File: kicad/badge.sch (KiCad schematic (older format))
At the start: 13 parts, among them IC1 ATMEGA328-P, P1 CONN_01X07, P2 9v battery, P3 FTDI programmer, SW1 SPST, U1 LM7805, Y1 16Mhz

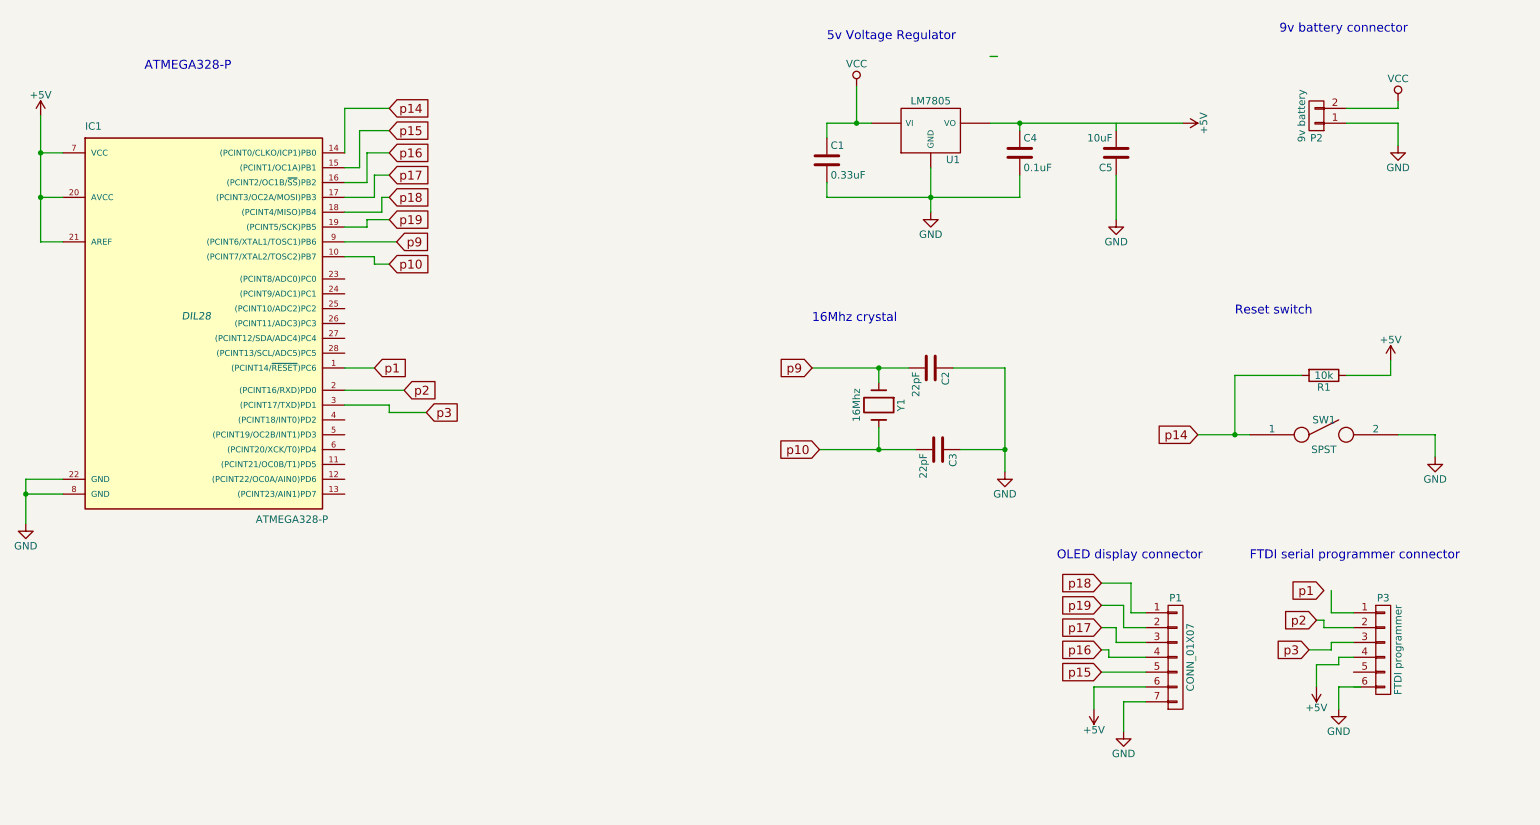
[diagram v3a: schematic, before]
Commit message: fix problems from rule check
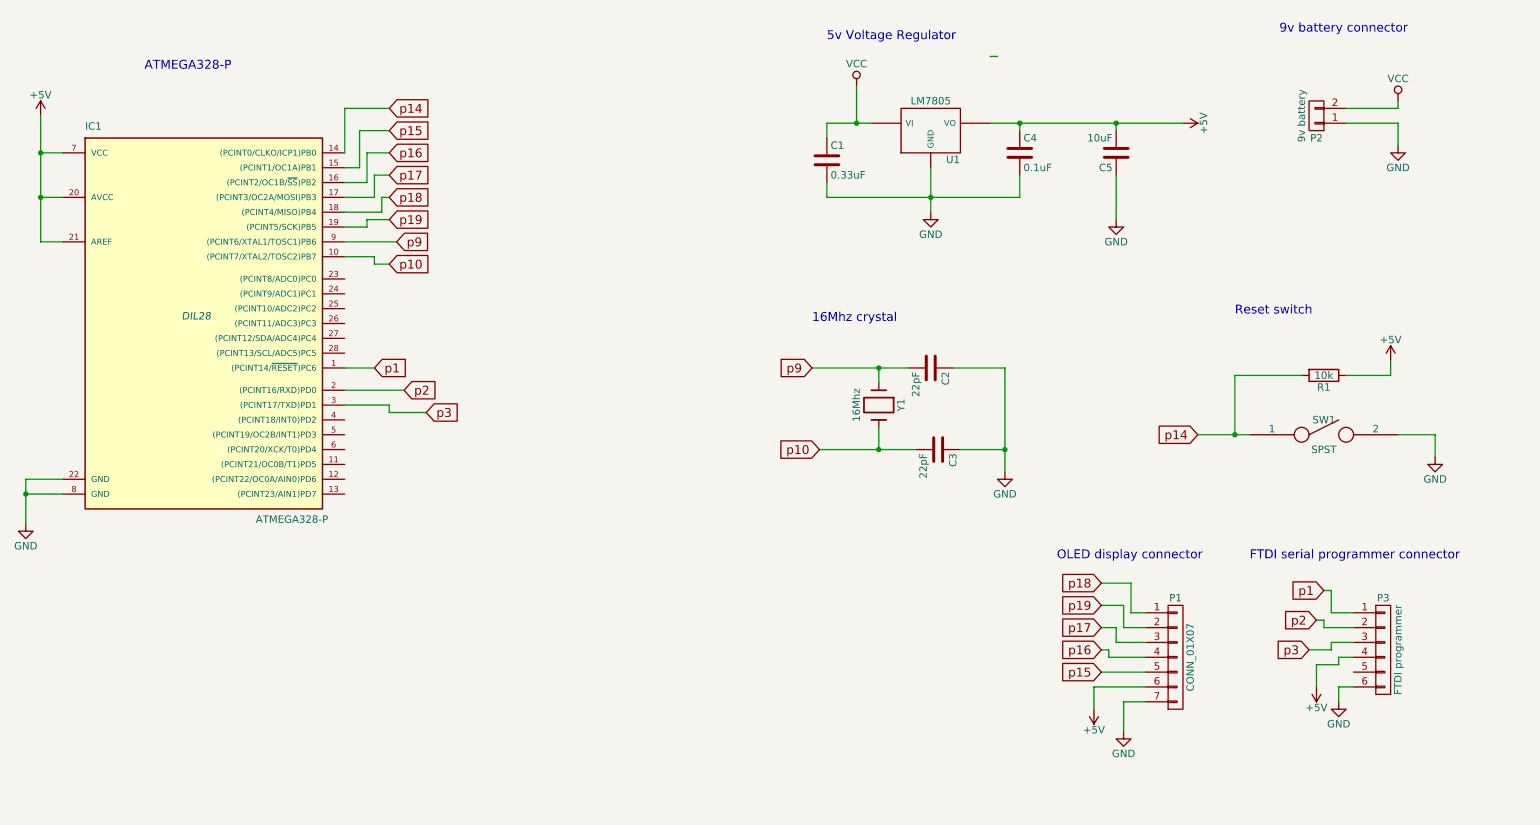
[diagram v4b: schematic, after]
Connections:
- wire segments 94 -> 107
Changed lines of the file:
@@
 L GND #PWR08
 U 1 1 58E1B9A0
-P 9950 5400
-F 0 "#PWR08" H 9950 5150 50  0001 C CNN
-F 1 "GND" H 9950 5250 50  0000 C CNN
-F 2 "" H 9950 5400 50  0000 C CNN
-F 3 "" H 9950 5400 50  0000 C CNN
-	1    9950 5400
+P 9950 5350
+F 0 "#PWR08" H 9950 5100 50  0001 C CNN
+F 1 "GND" H 9950 5200 50  0000 C CNN
+F 2 "" H 9950 5350 50  0000 C CNN
+F 3 "" H 9950 5350 50  0000 C CNN
+	1    9950 5350
 	1    0    0    -1
 $EndComp
@@
 	7350 3100 7700 3100
 Wire Wire Line
-	7700 3100 7700 3800
-Wire Wire Line
 	7400 3650 7700 3650
-Connection ~ 7700 3650
 Wire Wire Line
 	1350 3950 1100 3950
@@
 	8450 1800 8450 2100
 Wire Wire Line
-	9000 3550 9350 3550
+	9000 3550 9250 3550
+Wire Wire Line
+	9250 3550 9350 3550
 Wire Wire Line
 	9700 3150 9250 3150
@@
 	10300 3150 10000 3150
 Wire Wire Line
-	6500 1450 6800 1450
+	6500 1450 6700 1450
+Wire Wire Line
+	6700 1450 6800 1450
 Wire Wire Line
 	6500 1450 6500 1550
 Wire Wire Line
-	7200 1750 7200 2050
+	7200 1750 7200 1950
+Wire Wire Line
+	7200 1950 7200 2050
 Wire Wire Line
 	6500 1850 6500 1950
 Wire Wire Line
-	6500 1950 7800 1950
+	6500 1950 7200 1950
+Wire Wire Line
+	7200 1950 7800 1950
 Connection ~ 7200 1950
 Wire Wire Line
 	7800 1950 7800 1800
 Wire Wire Line
-	7600 1450 8900 1450
+	7600 1450 7800 1450
+Wire Wire Line
+	7800 1450 8450 1450
+Wire Wire Line
+	8450 1450 8900 1450
 Wire Wire Line
 	7800 1450 7800 1500
@@
 Wire Wire Line
 	10300 3050 10300 3150
-Wire Wire Line
-	6700 1200 6700 1450
 Connection ~ 6700 1450
 Connection ~ 6850 3100
 Connection ~ 6850 3650
 Wire Wire Line
-	1100 3850 1100 4150
+	1100 3850 1100 3950
+Wire Wire Line
+	1100 3950 1100 4150
 Wire Wire Line
 	10350 3550 10600 3550
@@
 	10000 1350 10350 1350
 Wire Wire Line
-	10350 1350 10350 1300
-Wire Wire Line
 	10000 1450 10350 1450
 Wire Wire Line
 	10350 1450 10350 1600
 Wire Wire Line
-	10100 5250 9950 5250
-Wire Wire Line
-	9950 5250 9950 5400
-Wire Wire Line
 	10600 3550 10600 3700
 Wire Wire Line
@@
 	9900 4600 9900 4750
 Wire Wire Line
-	9900 4750 10050 4750
-Wire Wire Line
 	9800 4800 9850 4800
 Wire Wire Line
@@
 Wire Wire Line
 	9950 5050 10050 5050
-Wire Wire Line
-	8450 1450 8450 1500
-Wire Wire Line
-	1200 2250 1350 2250
 Wire Wire Line
 	1200 1950 1350 1950
@@
 	1200 1650 1350 1650
 Wire Wire Line
-	1200 1400 1200 2250
+	1200 1400 1200 1650
+Wire Wire Line
+	1200 1650 1200 1950
+Wire Wire Line
+	1200 1950 1200 2250
 $Comp
 L +5V #PWR013
@@
 Reset switch
 Wire Wire Line
-	6400 3100 7050 3100
-Wire Wire Line
-	6450 3650 7100 3650
+	6400 3100 6850 3100
+Wire Wire Line
+	6850 3100 7050 3100
+Wire Wire Line
+	6450 3650 6850 3650
+Wire Wire Line
+	6850 3650 7100 3650
 $Comp
 L GND #PWR014
@@
 Wire Wire Line
 	3450 2400 3550 2400
+Wire Wire Line
+	7700 3100 7700 3650
+Wire Wire Line
+	7700 3650 7700 3800
+Connection ~ 7700 3650
+Wire Wire Line
+	10350 1350 10350 1300
+Wire Wire Line
+	8450 1450 8450 1500
+Connection ~ 8450 1450
+Wire Wire Line
+	9850 4600 9900 4600
+Wire Wire Line
+	10050 5250 9950 5250
+Wire Wire Line
+	9900 4750 10050 4750
+Wire Wire Line
+	1200 2250 1350 2250
+Wire Wire Line
+	6700 1200 6700 1450
+Wire Wire Line
+	9950 5250 9950 5350
 $EndSCHEMATC

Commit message: add LEDs
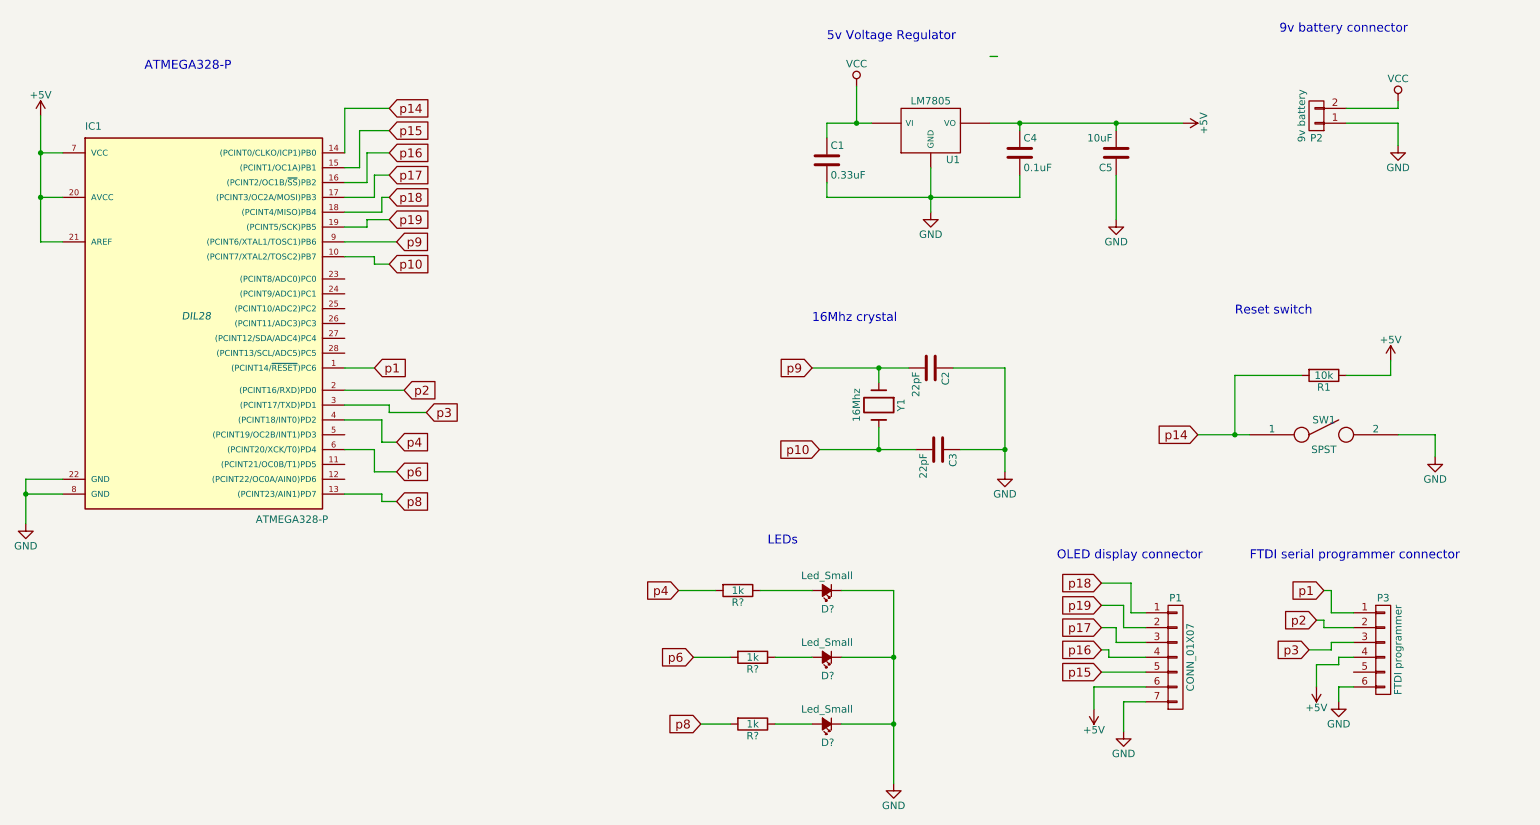
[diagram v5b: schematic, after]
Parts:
- added D? (x3): Led_Small, symbol Led_Small
- added R? (x3): 1k, symbol R
- C5: footprint (none) -> Capacitors_ThroughHole:C_Rect_L7_W2.5_P5
- P1: footprint (none) -> Pin_Headers:Pin_Header_Straight_1x07
- P2: footprint (none) -> Pin_Headers:Pin_Header_Straight_1x02
- P3: footprint (none) -> Pin_Headers:Pin_Header_Straight_1x06
- R1: footprint (none) -> Resistors_ThroughHole:Resistor_Horizontal_RM10mm
- SW1: footprint (none) -> Buttons_Switches_ThroughHole:SW_PUSH_SMALL
- Y1: footprint (none) -> Crystals:Crystal_HC49-U_Vertical
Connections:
- net GND: now also D?.1 (K), D?.1 (K), D?.1 (K)
- net p8: now reaches IC1.13 ((PCINT23/AIN1)PD7)
- net p8: now also R?.2
- net p4: now reaches IC1.4 ((PCINT18/INT0)PD2)
- net p4: now also R?.2
- net p6: now reaches IC1.6 ((PCINT20/XCK/T0)PD4)
- net p6: now also R?.2
- new net: D?.2 (A), R?.1 (x3)
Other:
- note added: "LEDs\n"
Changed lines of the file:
@@
 F 0 "R1" V 9930 3150 50  0000 C CNN
 F 1 "10k" V 9850 3150 50  0000 C CNN
-F 2 "" V 9780 3150 50  0000 C CNN
+F 2 "Resistors_ThroughHole:Resistor_Horizontal_RM10mm" V 9780 3150 50  0001 C CNN
 F 3 "" H 9850 3150 50  0000 C CNN
 	1    9850 3150
@@
 F 0 "C2" H 7225 3200 50  0000 L CNN
 F 1 "22pF" H 7225 3000 50  0000 L CNN
-F 2 "" H 7238 2950 50  0000 C CNN
+F 2 "" H 7238 2950 50  0001 C CNN
 F 3 "" H 7200 3100 50  0000 C CNN
 	1    7200 3100
@@
 F 0 "C5" H 8475 1750 50  0000 L CNN
 F 1 "10uF" H 8475 1550 50  0000 L CNN
-F 2 "" H 8488 1500 50  0000 C CNN
+F 2 "Capacitors_ThroughHole:C_Rect_L7_W2.5_P5" H 8488 1500 50  0001 C CNN
 F 3 "" H 8450 1650 50  0000 C CNN
 	1    8450 1650
@@
 F 0 "SW1" H 9850 3650 50  0000 C CNN
 F 1 "SPST" H 9850 3450 50  0000 C CNN
-F 2 "" H 9850 3550 50  0000 C CNN
+F 2 "Buttons_Switches_ThroughHole:SW_PUSH_SMALL" H 9850 3550 50  0001 C CNN
 F 3 "" H 9850 3550 50  0000 C CNN
 	1    9850 3550
@@
 F 0 "U1" H 7350 1304 50  0000 C CNN
 F 1 "LM7805" H 7200 1700 50  0000 C CNN
-F 2 "" H 7200 1500 50  0000 C CNN
+F 2 "" H 7200 1500 50  0001 C CNN
 F 3 "" H 7200 1500 50  0000 C CNN
 	1    7200 1500
@@
 F 0 "C4" H 7825 1750 50  0000 L CNN
 F 1 "0.1uF" H 7825 1550 50  0000 L CNN
-F 2 "" H 7838 1500 50  0000 C CNN
+F 2 "" H 7838 1500 50  0001 C CNN
 F 3 "" H 7800 1650 50  0000 C CNN
 	1    7800 1650
@@
 F 0 "C1" H 6525 1800 50  0000 L CNN
 F 1 "0.33uF" H 6525 1600 50  0000 L CNN
-F 2 "" H 6538 1550 50  0000 C CNN
+F 2 "" H 6538 1550 50  0001 C CNN
 F 3 "" H 6500 1700 50  0000 C CNN
 	1    6500 1700
@@
 F 0 "P2" H 9800 1550 50  0000 C CNN
 F 1 "9v battery " V 9900 1400 50  0000 C CNN
-F 2 "" H 9800 1400 50  0000 C CNN
+F 2 "Pin_Headers:Pin_Header_Straight_1x02" H 9800 1400 50  0001 C CNN
 F 3 "" H 9800 1400 50  0000 C CNN
 	1    9800 1400
@@
 F 0 "P3" H 10250 5350 50  0000 C CNN
 F 1 "FTDI programmer" V 10350 5000 50  0000 C CNN
-F 2 "" H 10250 5000 50  0000 C CNN
+F 2 "Pin_Headers:Pin_Header_Straight_1x06" H 10250 5000 50  0001 C CNN
 F 3 "" H 10250 5000 50  0000 C CNN
 	1    10250 5000
@@
 F 0 "Y1" H 6850 3500 50  0000 C CNN
 F 1 "16Mhz" H 6850 3200 50  0000 C CNN
-F 2 "" H 6850 3350 50  0000 C CNN
+F 2 "Crystals:Crystal_HC49-U_Vertical" H 6850 3350 50  0001 C CNN
 F 3 "" H 6850 3350 50  0000 C CNN
 	1    6850 3350
@@
 F 0 "C3" H 7275 3750 50  0000 L CNN
 F 1 "22pF" H 7275 3550 50  0000 L CNN
-F 2 "" H 7288 3500 50  0000 C CNN
+F 2 "" H 7288 3500 50  0001 C CNN
 F 3 "" H 7250 3650 50  0000 C CNN
 	1    7250 3650
@@
 	8450 1800 8450 2100
 Wire Wire Line
-	9000 3550 9250 3550
-Wire Wire Line
-	9250 3550 9350 3550
+	9000 3550 9350 3550
 Wire Wire Line
 	9700 3150 9250 3150
@@
 	10300 3150 10000 3150
 Wire Wire Line
-	6500 1450 6700 1450
-Wire Wire Line
-	6700 1450 6800 1450
+	6500 1450 6800 1450
 Wire Wire Line
 	6500 1450 6500 1550
 Wire Wire Line
-	7200 1750 7200 1950
-Wire Wire Line
-	7200 1950 7200 2050
+	7200 1750 7200 2050
 Wire Wire Line
 	6500 1850 6500 1950
 Wire Wire Line
-	6500 1950 7200 1950
-Wire Wire Line
-	7200 1950 7800 1950
+	6500 1950 7800 1950
 Connection ~ 7200 1950
 Wire Wire Line
 	7800 1950 7800 1800
 Wire Wire Line
-	7600 1450 7800 1450
-Wire Wire Line
-	7800 1450 8450 1450
-Wire Wire Line
-	8450 1450 8900 1450
+	7600 1450 8900 1450
 Wire Wire Line
 	7800 1450 7800 1500
@@
 Connection ~ 6850 3650
 Wire Wire Line
-	1100 3850 1100 3950
-Wire Wire Line
-	1100 3950 1100 4150
+	1100 3850 1100 4150
 Wire Wire Line
 	10350 3550 10600 3550
@@
 	1200 1650 1350 1650
 Wire Wire Line
-	1200 1400 1200 1650
-Wire Wire Line
-	1200 1650 1200 1950
-Wire Wire Line
-	1200 1950 1200 2250
+	1200 1400 1200 2250
 $Comp
 L +5V #PWR013
@@
 Reset switch
 Wire Wire Line
-	6400 3100 6850 3100
-Wire Wire Line
-	6850 3100 7050 3100
-Wire Wire Line
-	6450 3650 6850 3650
-Wire Wire Line
-	6850 3650 7100 3650
+	6400 3100 7050 3100
+Wire Wire Line
+	6450 3650 7100 3650
 $Comp
 L GND #PWR014
@@
 F 0 "P1" H 8850 5450 50  0000 C CNN
 F 1 "CONN_01X07" V 8950 5050 50  0000 C CNN
-F 2 "" H 8850 5050 50  0000 C CNN
+F 2 "Pin_Headers:Pin_Header_Straight_1x07" H 8850 5050 50  0001 C CNN
 F 3 "" H 8850 5050 50  0000 C CNN
 	1    8850 5050
@@
 	3450 2400 3550 2400
 Wire Wire Line
-	7700 3100 7700 3650
-Wire Wire Line
-	7700 3650 7700 3800
+	7700 3100 7700 3800
 Connection ~ 7700 3650
 Wire Wire Line
@@
 Wire Wire Line
 	9950 5250 9950 5350
+Text GLabel 3600 3600 2    60   Input ~ 0
+p4
+Text GLabel 3600 3800 2    60   Input ~ 0
+p6
+Text GLabel 3600 4000 2    60   Input ~ 0
+p8
+Wire Wire Line
+	3250 3450 3500 3450
+Wire Wire Line
+	3500 3450 3500 3600
+Wire Wire Line
+	3500 3600 3600 3600
+Wire Wire Line
+	3250 3650 3450 3650
+Wire Wire Line
+	3450 3650 3450 3800
+Wire Wire Line
+	3450 3800 3600 3800
+Wire Wire Line
+	3250 3950 3500 3950
+Wire Wire Line
+	3500 3950 3500 4000
+Wire Wire Line
+	3500 4000 3600 4000
+$Comp
+L Led_Small D?
+U 1 1 58F40DF3
+P 6500 4600
+F 0 "D?" H 6450 4725 50  0000 L CNN
+F 1 "Led_Small" H 6325 4500 50  0000 L CNN
+F 2 "" V 6500 4600 50  0000 C CNN
+F 3 "" V 6500 4600 50  0000 C CNN
+	1    6500 4600
+	-1   0    0    1
+$EndComp
+$Comp
+L Led_Small D?
+U 1 1 58F40E6E
+P 6500 5050
+F 0 "D?" H 6450 5175 50  0000 L CNN
+F 1 "Led_Small" H 6325 4950 50  0000 L CNN
+F 2 "" V 6500 5050 50  0000 C CNN
+F 3 "" V 6500 5050 50  0000 C CNN
+	1    6500 5050
+	-1   0    0    1
+$EndComp
+$Comp
+L Led_Small D?
+U 1 1 58F40EC6
+P 6500 5500
+F 0 "D?" H 6450 5625 50  0000 L CNN
+F 1 "Led_Small" H 6325 5400 50  0000 L CNN
+F 2 "" V 6500 5500 50  0000 C CNN
+F 3 "" V 6500 5500 50  0000 C CNN
+	1    6500 5500
+	-1   0    0    1
+$EndComp
+$Comp
+L GND #PWR?
+U 1 1 58F41237
+P 6950 5900
+F 0 "#PWR?" H 6950 5650 50  0001 C CNN
+F 1 "GND" H 6950 5750 50  0000 C CNN
+F 2 "" H 6950 5900 50  0000 C CNN
+F 3 "" H 6950 5900 50  0000 C CNN
+	1    6950 5900
+	1    0    0    -1
+$EndComp
+Wire Wire Line
+	6600 4600 6950 4600
+Wire Wire Line
+	6950 4600 6950 5900
+Wire Wire Line
+	6600 5050 6950 5050
+Connection ~ 6950 5050
+Wire Wire Line
+	6600 5500 6950 5500
+Connection ~ 6950 5500
+Text GLabel 5500 4600 0    60   Input ~ 0
+p4
+Text GLabel 5600 5050 0    60   Input ~ 0
+p6
+Text GLabel 5650 5500 0    60   Input ~ 0
+p8
+Text Notes 6100 4300 0    60   ~ 0
+LEDs\n
+$Comp
+L R R?
+U 1 1 58F42636
+P 5900 4600
+F 0 "R?" V 5980 4600 50  0000 C CNN
+F 1 "1k" V 5900 4600 50  0000 C CNN
+F 2 "" V 5830 4600 50  0000 C CNN
+F 3 "" H 5900 4600 50  0000 C CNN
+	1    5900 4600
+	0    1    1    0
+$EndComp
+$Comp
+L R R?
+U 1 1 58F427B6
+P 6000 5050
+F 0 "R?" V 6080 5050 50  0000 C CNN
+F 1 "1k" V 6000 5050 50  0000 C CNN
+F 2 "" V 5930 5050 50  0000 C CNN
+F 3 "" H 6000 5050 50  0000 C CNN
+	1    6000 5050
+	0    1    1    0
+$EndComp
+$Comp
+L R R?
+U 1 1 58F42812
+P 6000 5500
+F 0 "R?" V 6080 5500 50  0000 C CNN
+F 1 "1k" V 6000 5500 50  0000 C CNN
+F 2 "" V 5930 5500 50  0000 C CNN
+F 3 "" H 6000 5500 50  0000 C CNN
+	1    6000 5500
+	0    1    1    0
+$EndComp
+Wire Wire Line
+	5500 4600 5750 4600
+Wire Wire Line
+	6050 4600 6400 4600
+Wire Wire Line
+	5600 5050 5850 5050
+Wire Wire Line
+	6150 5050 6400 5050
+Wire Wire Line
+	5650 5500 5850 5500
+Wire Wire Line
+	6150 5500 6400 5500
 $EndSCHEMATC
